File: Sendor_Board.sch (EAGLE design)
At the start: 22 parts, among them Q1 8.000Mhz, U1 PIC32MX795F512H-80I/PT, U2 SHT25, X1 MINI-USB-SHIELD-UX60A-MB-5ST

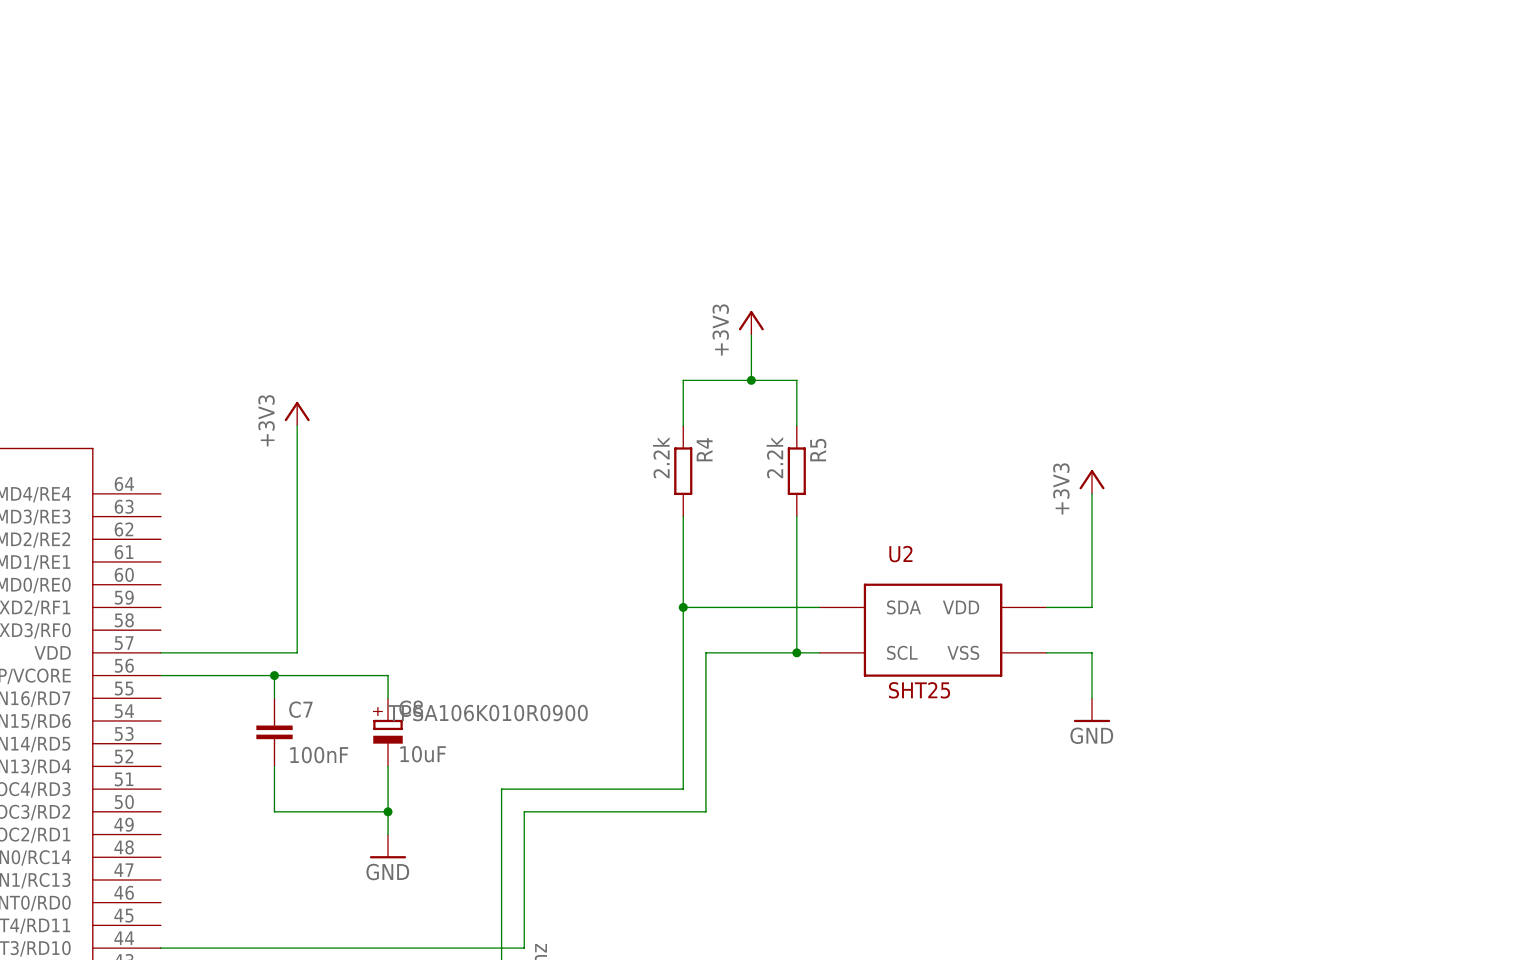
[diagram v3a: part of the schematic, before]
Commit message: Add MPL115A2 to schematic
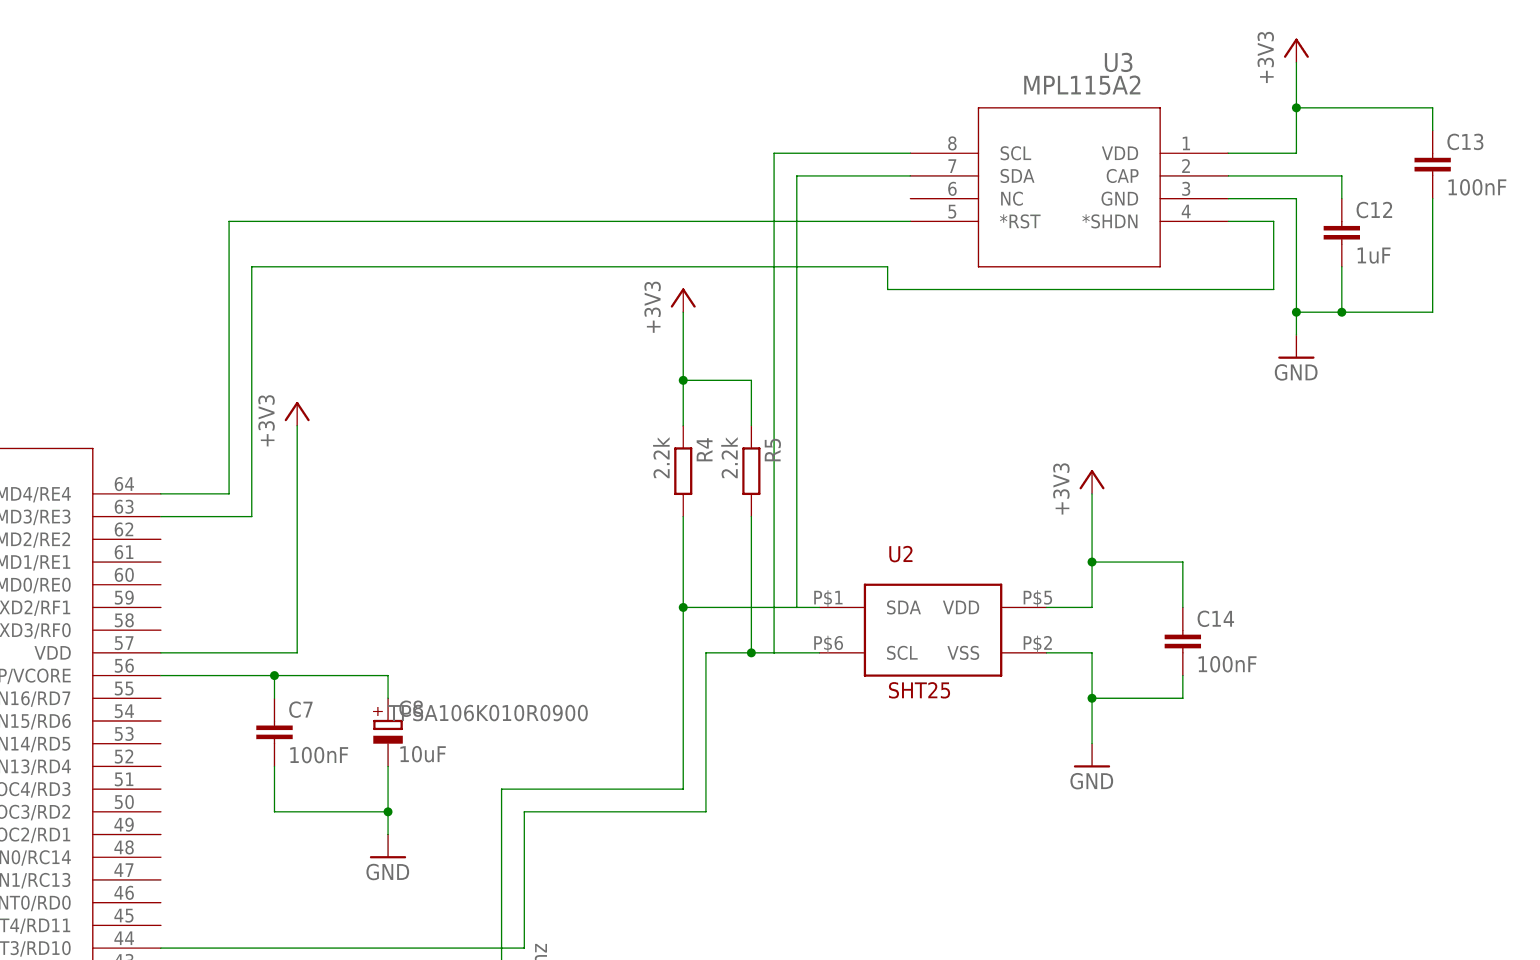
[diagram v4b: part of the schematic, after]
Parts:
- added C12: 1uF, resistor:C-EUC1206K
- added C13, C14: 100nF, resistor:C-EUC1206K
- added U3: MPL115A2, pfo:MPL115A2
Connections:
- new net N$13: C12.1, U3.CAP
- new net N$14: U1.ERXERR/PMD4/RE4, U3.*RST
- new net N$15: U1.ERXCLK/PMD3/RE3, U3.*SHDN
- net +3V3: now also C13.1, C14.1, U3.VDD
- net GND: now also C12.2, C13.2, C14.2, U3.GND
- net N$11: now also U3.SDA
- net N$12: now also U3.SCL
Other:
- moved on the sheet: R5
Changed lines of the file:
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@@
 <part name="R5" library="resistor" deviceset="R-EU_" device="R1206" value="2.2k"/>
 <part name="+3V3" library="supply1" deviceset="+3V3" device=""/>
+<part name="U3" library="pfo" deviceset="MPL115A2" device=""/>
+<part name="+3V4" library="supply1" deviceset="+3V3" device=""/>
+<part name="GND9" library="supply1" deviceset="GND" device=""/>
+<part name="C12" library="resistor" deviceset="C-EU" device="C1206K" value="1uF"/>
+<part name="C13" library="resistor" deviceset="C-EU" device="C1206K" value="100nF"/>
+<part name="C14" library="resistor" deviceset="C-EU" device="C1206K" value="100nF"/>
 </parts>
 <sheets>
@@
 <instance part="X1" gate="G$1" x="215.9" y="-40.64"/>
 <instance part="U2" gate="G$1" x="233.68" y="68.58"/>
-<instance part="GND8" gate="1" x="251.46" y="58.42"/>
+<instance part="GND8" gate="1" x="251.46" y="53.34"/>
 <instance part="+3V2" gate="G$1" x="251.46" y="86.36"/>
 <instance part="U1" gate="A" x="0" y="83.82"/>
 <instance part="R4" gate="G$1" x="205.74" y="86.36" rot="R270"/>
-<instance part="R5" gate="G$1" x="218.44" y="86.36" rot="R270"/>
-<instance part="+3V3" gate="G$1" x="213.36" y="104.14"/>
+<instance part="R5" gate="G$1" x="213.36" y="86.36" rot="R270"/>
+<instance part="+3V3" gate="G$1" x="205.74" y="106.68"/>
+<instance part="U3" gate="A" x="266.7" y="121.92" rot="MR0"/>
+<instance part="+3V4" gate="G$1" x="274.32" y="134.62"/>
+<instance part="GND9" gate="1" x="274.32" y="99.06"/>
+<instance part="C12" gate="G$1" x="279.4" y="114.3"/>
+<instance part="C13" gate="G$1" x="289.56" y="121.92"/>
+<instance part="C14" gate="G$1" x="261.62" y="68.58"/>
 </instances>
 <busses>
@@
 <wire x1="246.38" y1="66.04" x2="251.46" y2="66.04" width="0.1524" layer="91"/>
 <wire x1="251.46" y1="66.04" x2="251.46" y2="60.96" width="0.1524" layer="91"/>
+<pinref part="C14" gate="G$1" pin="2"/>
+<wire x1="251.46" y1="60.96" x2="251.46" y2="55.88" width="0.1524" layer="91"/>
+<wire x1="261.62" y1="63.5" x2="261.62" y2="60.96" width="0.1524" layer="91"/>
+<wire x1="261.62" y1="60.96" x2="251.46" y2="60.96" width="0.1524" layer="91"/>
+<junction x="251.46" y="60.96"/>
+</segment>
+<segment>
+<pinref part="U3" gate="A" pin="GND"/>
+<pinref part="GND9" gate="1" pin="GND"/>
+<wire x1="266.7" y1="116.84" x2="274.32" y2="116.84" width="0.1524" layer="91"/>
+<wire x1="274.32" y1="116.84" x2="274.32" y2="104.14" width="0.1524" layer="91"/>
+<pinref part="C13" gate="G$1" pin="2"/>
+<wire x1="274.32" y1="104.14" x2="274.32" y2="101.6" width="0.1524" layer="91"/>
+<wire x1="289.56" y1="116.84" x2="289.56" y2="104.14" width="0.1524" layer="91"/>
+<wire x1="289.56" y1="104.14" x2="279.4" y2="104.14" width="0.1524" layer="91"/>
+<pinref part="C12" gate="G$1" pin="2"/>
+<wire x1="279.4" y1="104.14" x2="274.32" y2="104.14" width="0.1524" layer="91"/>
+<wire x1="279.4" y1="109.22" x2="279.4" y2="104.14" width="0.1524" layer="91"/>
+<junction x="279.4" y="104.14"/>
+<junction x="274.32" y="104.14"/>
 </segment>
 </net>
@@
 <pinref part="+3V2" gate="G$1" pin="+3V3"/>
 <wire x1="246.38" y1="71.12" x2="251.46" y2="71.12" width="0.1524" layer="91"/>
-<wire x1="251.46" y1="71.12" x2="251.46" y2="83.82" width="0.1524" layer="91"/>
+<wire x1="251.46" y1="71.12" x2="251.46" y2="76.2" width="0.1524" layer="91"/>
+<pinref part="C14" gate="G$1" pin="1"/>
+<wire x1="251.46" y1="76.2" x2="251.46" y2="83.82" width="0.1524" layer="91"/>
+<wire x1="261.62" y1="71.12" x2="261.62" y2="76.2" width="0.1524" layer="91"/>
+<wire x1="261.62" y1="76.2" x2="251.46" y2="76.2" width="0.1524" layer="91"/>
+<junction x="251.46" y="76.2"/>
 </segment>
 <segment>
@@
 <pinref part="R5" gate="G$1" pin="1"/>
 <wire x1="205.74" y1="96.52" x2="213.36" y2="96.52" width="0.1524" layer="91"/>
-<wire x1="213.36" y1="96.52" x2="218.44" y2="96.52" width="0.1524" layer="91"/>
-<wire x1="218.44" y1="96.52" x2="218.44" y2="91.44" width="0.1524" layer="91"/>
+<wire x1="213.36" y1="96.52" x2="213.36" y2="91.44" width="0.1524" layer="91"/>
 <pinref part="+3V3" gate="G$1" pin="+3V3"/>
-<wire x1="213.36" y1="101.6" x2="213.36" y2="96.52" width="0.1524" layer="91"/>
-<junction x="213.36" y="96.52"/>
+<wire x1="205.74" y1="104.14" x2="205.74" y2="96.52" width="0.1524" layer="91"/>
+<junction x="205.74" y="96.52"/>
+</segment>
+<segment>
+<pinref part="U3" gate="A" pin="VDD"/>
+<pinref part="+3V4" gate="G$1" pin="+3V3"/>
+<wire x1="266.7" y1="121.92" x2="274.32" y2="121.92" width="0.1524" layer="91"/>
+<wire x1="274.32" y1="121.92" x2="274.32" y2="127" width="0.1524" layer="91"/>
+<pinref part="C13" gate="G$1" pin="1"/>
+<wire x1="274.32" y1="127" x2="274.32" y2="132.08" width="0.1524" layer="91"/>
+<wire x1="289.56" y1="124.46" x2="289.56" y2="127" width="0.1524" layer="91"/>
+<wire x1="289.56" y1="127" x2="274.32" y2="127" width="0.1524" layer="91"/>
+<junction x="274.32" y="127"/>
 </segment>
 </net>
@@
 <wire x1="205.74" y1="50.8" x2="205.74" y2="71.12" width="0.1524" layer="91"/>
 <pinref part="U2" gate="G$1" pin="SDA"/>
-<wire x1="220.98" y1="71.12" x2="205.74" y2="71.12" width="0.1524" layer="91"/>
+<wire x1="220.98" y1="71.12" x2="218.44" y2="71.12" width="0.1524" layer="91"/>
+<wire x1="218.44" y1="71.12" x2="205.74" y2="71.12" width="0.1524" layer="91"/>
 <wire x1="205.74" y1="71.12" x2="205.74" y2="81.28" width="0.1524" layer="91"/>
 <junction x="205.74" y="71.12"/>
 <pinref part="R4" gate="G$1" pin="2"/>
+<pinref part="U3" gate="A" pin="SDA"/>
+<wire x1="218.44" y1="71.12" x2="218.44" y2="119.38" width="0.1524" layer="91"/>
+<wire x1="218.44" y1="119.38" x2="231.14" y2="119.38" width="0.1524" layer="91"/>
 </segment>
 </net>
@@
 <wire x1="208.28" y1="48.26" x2="208.28" y2="66.04" width="0.1524" layer="91"/>
 <pinref part="U2" gate="G$1" pin="SCL"/>
-<wire x1="208.28" y1="66.04" x2="218.44" y2="66.04" width="0.1524" layer="91"/>
-<wire x1="220.98" y1="66.04" x2="218.44" y2="66.04" width="0.1524" layer="91"/>
-<wire x1="218.44" y1="66.04" x2="218.44" y2="81.28" width="0.1524" layer="91"/>
-<junction x="218.44" y="66.04"/>
+<wire x1="208.28" y1="66.04" x2="213.36" y2="66.04" width="0.1524" layer="91"/>
+<wire x1="220.98" y1="66.04" x2="215.9" y2="66.04" width="0.1524" layer="91"/>
+<wire x1="215.9" y1="66.04" x2="213.36" y2="66.04" width="0.1524" layer="91"/>
+<wire x1="213.36" y1="66.04" x2="213.36" y2="81.28" width="0.1524" layer="91"/>
+<junction x="213.36" y="66.04"/>
 <pinref part="R5" gate="G$1" pin="2"/>
-</segment>
-</net>
+<pinref part="U3" gate="A" pin="SCL"/>
+<wire x1="215.9" y1="66.04" x2="215.9" y2="121.92" width="0.1524" layer="91"/>
+<wire x1="215.9" y1="121.92" x2="231.14" y2="121.92" width="0.1524" layer="91"/>
+</segment>
+</net>
+<net name="N$13" class="0">
+<segment>
+<pinref part="U3" gate="A" pin="CAP"/>
+<pinref part="C12" gate="G$1" pin="1"/>
+<wire x1="266.7" y1="119.38" x2="279.4" y2="119.38" width="0.1524" layer="91"/>
+<wire x1="279.4" y1="119.38" x2="279.4" y2="116.84" width="0.1524" layer="91"/>
+</segment>
+</net>
+<net name="N$14" class="0">
+<segment>
+<pinref part="U1" gate="A" pin="ERXERR/PMD4/RE4"/>
+<wire x1="147.32" y1="83.82" x2="154.94" y2="83.82" width="0.1524" layer="91"/>
+<wire x1="154.94" y1="83.82" x2="154.94" y2="114.3" width="0.1524" layer="91"/>
+<pinref part="U3" gate="A" pin="*RST"/>
+<wire x1="154.94" y1="114.3" x2="231.14" y2="114.3" width="0.1524" layer="91"/>
+</segment>
+</net>
+<net name="N$15" class="0">
+<segment>
+<pinref part="U1" gate="A" pin="ERXCLK/PMD3/RE3"/>
+<wire x1="147.32" y1="81.28" x2="157.48" y2="81.28" width="0.1524" layer="91"/>
+<wire x1="157.48" y1="81.28" x2="157.48" y2="109.22" width="0.1524" layer="91"/>
+<wire x1="157.48" y1="109.22" x2="228.6" y2="109.22" width="0.1524" layer="91"/>
+<wire x1="228.6" y1="109.22" x2="228.6" y2="106.68" width="0.1524" layer="91"/>
+<wire x1="228.6" y1="106.68" x2="271.78" y2="106.68" width="0.1524" layer="91"/>
+<wire x1="271.78" y1="106.68" x2="271.78" y2="114.3" width="0.1524" layer="91"/>
+<pinref part="U3" gate="A" pin="*SHDN"/>
+<wire x1="271.78" y1="114.3" x2="266.7" y2="114.3" width="0.1524" layer="91"/>
+</segment>
+</net>

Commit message: Change placement
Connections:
- net N$10 renamed D-
- net N$14 renamed RST_PRES
- net N$15 renamed SHD_PRES
- net N$8 renamed USBID
- net N$9 renamed D+
- removed net N$11: R4.2, U1.AERXD0/ETXD2/*SS1A/U1BRX/*U1ACTS/SDA1/IC2/INT2/RD9, U2.SDA, U3.SDA
- removed net N$12: R5.2, U1.ECOL/AERXDV/SCL1/IC3/PMCS2/PMA15/INT3/RD10, U2.SCL, U3.SCL
- new net SCL_CAP: R4.2, U1.ECOL/AERXDV/SCL1/IC3/PMCS2/PMA15/INT3/RD10, U2.SCL, U3.SCL
- new net SDA_CAP: R5.2, U1.AERXD0/ETXD2/*SS1A/U1BRX/*U1ACTS/SDA1/IC2/INT2/RD9, U2.SDA, U3.SDA
- net +3V3: now also U1.VDD_4
- net GND: no longer U1.VDD_4
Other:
- moved on the sheet: C10, C11, C12, C13, C14, C7, C8, Q1, R4, R5, U2, U3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
